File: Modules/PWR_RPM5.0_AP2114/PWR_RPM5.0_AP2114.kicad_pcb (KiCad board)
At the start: 4 copper layers, 39.9 x 52.7 mm, 30 parts, among them J1 Screw Terminal, J5 2.54 Pins, J6 2.54 Pins, J8 Red/Black PowerPole 45, J9 2.54mm Header, SW1 SW_SP3T, SW2 SPST, U1 RPM5.0-2.0, U2 AP2114HA-3.3

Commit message: Silkscreen tweaks
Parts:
- moved G*** 7.23 mm to (168.9, 87.6)
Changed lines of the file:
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@@
 	(footprint "libraries:Logo_10mm_inv"
 		(layer "B.Cu")
-		(at 176.149 87.630467 -90)
+		(at 168.914248 87.630467 -90)
 		(property "Reference" "G***"
 			(at 0 0 90)

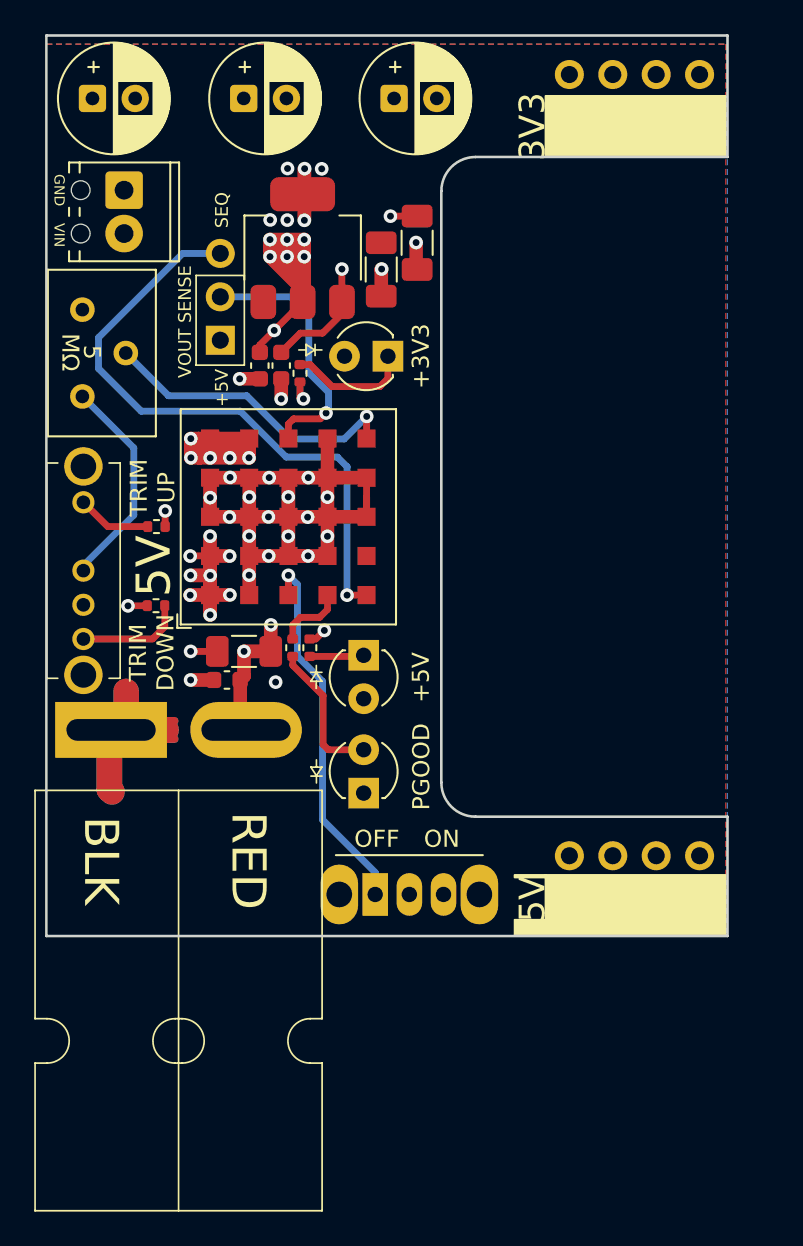
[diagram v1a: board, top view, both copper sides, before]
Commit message: Corrected breadboard width
Gave me a chance to rearrange some of the 3V3 stuff, looks much healthier now
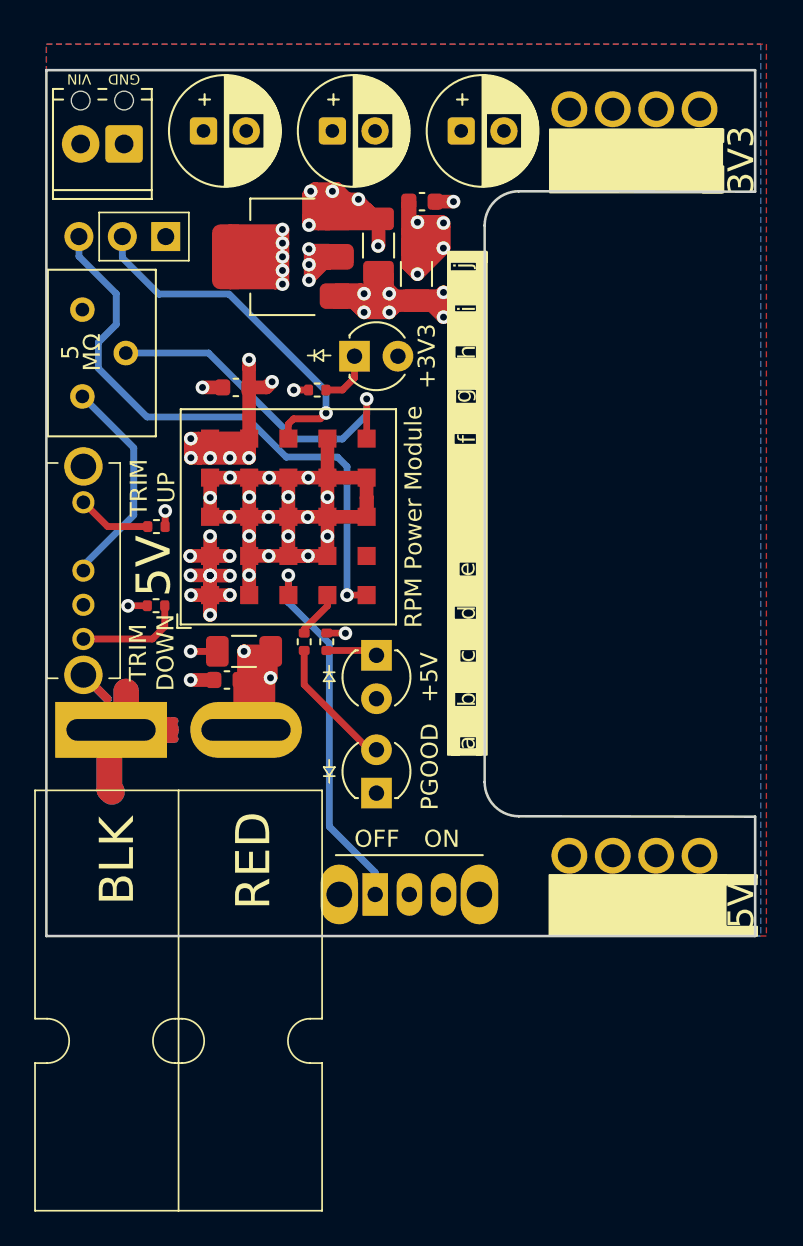
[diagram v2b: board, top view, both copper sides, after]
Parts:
- G***: footprint libraries:Logo_10mm_inv -> libraries:Logo_15mm
- S1: footprint Connector_PinHeader_1.00mm:PinHeader_1x01_P1.00mm_Horizontal -> libraries:Breadboard_400
- moved S1 15.2 mm to (184.1, 102.6)
- moved C13 13.5 mm to (179.3, 70.9), turned to 0 degrees
- moved J9 6.85 mm to (164.3, 73.0), turned to -90 degrees
- moved C5 6.77 mm to (166.5, 66.8)
- moved C7 5.53 mm to (174.1, 66.8)
- moved C8 4.36 mm to (181.6, 66.8)
- moved C11 2.95 mm to (168.4, 81.8), turned to 180 degrees
- moved J1 2.70 mm to (161.9, 67.6), turned to 180 degrees
- moved J6 2.03 mm to (188.0, 65.5)
- moved D3 1.95 mm to (175.4, 80.0), turned to 0 degrees
- moved C12 1.82 mm to (179.0, 75.2), turned to -90 degrees
- moved C10 1.41 mm to (176.8, 73.5), turned to -90 degrees
- moved R5 1.41 mm to (173.2, 82.0), turned to 180 degrees
- moved U2 1.26 mm to (171.2, 74.2), turned to 180 degrees
- moved G*** 1.18 mm to (170.1, 87.6)
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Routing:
- net GND: track 152.3 -> 211.4 mm, vias 31 -> 34
- net +5V0: track 23.4 -> 46.0 mm, vias 8 -> 13
- net /PWR_IN: track 29.8 -> 40.7 mm, vias 10 -> 12
- net Net-(J9-Pin_2): track 15.2 -> 21.0 mm
- net Net-(D3-K): track 7.18 -> 3.24 mm
- net +3V3: track 28.6 -> 32.0 mm, vias 8 -> 7
- net Net-(U1-Trim): track 18.0 -> 20.1 mm
- net Net-(J9-Pin_3): track 36.6 -> 34.7 mm
- net Net-(U1-PGood): track 4.07 -> 2.79 mm
- net Net-(D1-A): track 8.39 -> 7.85 mm
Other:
- board size 39.9 x 52.7 mm -> 41.5 x 50.7 mm
- board text added: "RPM Power Module"
- board text added: "SHORT FOR"
- board text added: "a"
- board text added: "b"
- board text added: "c"
- board text added: "d"
- board text added: "e"
- board text added: "f"
- board text added: "g"
- board text added: "h"
- board text added: "i"
- board text added: "j"
